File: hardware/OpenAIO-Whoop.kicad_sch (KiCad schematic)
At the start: 0 parts

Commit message: WIP schematic verify (D113): pre-shunt battery node +BATT_IN becomes /POWER/CSA+ (VBAT class) for the lineup power-net style; DRU regenerated; verifier mid-run, not yet final
Co-Authored-By: Claude Opus 5.5 <noreply@anthropic.com>
Claude-Session: https://claude.ai/code/session_01RFaS5jnC9tnPam9GBgmGnG
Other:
- note added: "BATTERY PADS TVS + SHUNT INA186 CURRENT 5V BOOST USB OVP 5V MUX 3V3 LDO CAM 5V FILTER O4 HD SWITCH"
- note added: "MOTOR LANDS LED / BUZZER CAMERA HD (O4) USB JST SH"
- note removed: "BATTERY MOTOR LANDS LED / BUZZER CAMERA HD (O4) USB JST SH"
- note removed: "TVS + SHUNT INA186 CURRENT 5V BOOST USB OVP 5V MUX 3V3 LDO CAM 5V FILTER O4 HD SWITCH"
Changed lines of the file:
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@@
 		)
 	)
-	(text "TVS + SHUNT\nINA186 CURRENT\n5V BOOST\nUSB OVP\n5V MUX\n3V3 LDO\nCAM 5V FILTER\nO4 HD SWITCH"
+	(text "BATTERY PADS\nTVS + SHUNT\nINA186 CURRENT\n5V BOOST\nUSB OVP\n5V MUX\n3V3 LDO\nCAM 5V FILTER\nO4 HD SWITCH"
 		(exclude_from_sim no)
 		(at 20.32 34.29 0)
@@
 		)
 	)
-	(text "BATTERY\nMOTOR LANDS\nLED / BUZZER\nCAMERA\nHD (O4)\nUSB JST SH"
+	(text "MOTOR LANDS\nLED / BUZZER\nCAMERA\nHD (O4)\nUSB JST SH"
 		(exclude_from_sim no)
 		(at 378.46 34.29 0)
@@
 				)
 			)
-			(table_cell "+BATT_IN"
+			(table_cell "CSA+"
 				(exclude_from_sim no)
 				(at 17.78 215.9 0)

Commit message: Schematic fixes: RP2350 UART net names match the hardware UARTs (UART1 on GPIO8/9 = CRSF to the ESP32, UART0 on GPIO16/17 = TX1/RX1 pads); VTX_PWR_CTL on ESP32 GPIO4 (reset pull-down) gets R68 10k pull-up / R84 270R so stock ELRS keeps the VTX on; docs; verify pending
Co-Authored-By: Claude Opus 5.5 <noreply@anthropic.com>
Claude-Session: https://claude.ai/code/session_01RFaS5jnC9tnPam9GBgmGnG
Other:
- sheet PADS ports: added UART0_RX, UART0_TX; removed UART1_RX, UART1_TX
- sheet RX ports: added UART1_RX, UART1_TX; removed UART0_RX, UART0_TX
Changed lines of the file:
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@@
 		)
 	)
-	(label "UART0_TX"
+	(label "UART1_TX"
 		(at 200.66 35.56 0)
 		(effects
@@
 		)
 	)
-	(label "UART1_RX"
+	(label "UART0_RX"
 		(at 358.14 182.88 180)
 		(effects
@@
 		)
 	)
-	(label "UART1_TX"
+	(label "UART0_TX"
 		(at 200.66 180.34 0)
 		(effects
@@
 		)
 	)
-	(label "UART0_RX"
+	(label "UART1_RX"
 		(at 220.98 38.1 180)
 		(effects
@@
 			)
 		)
-		(pin "UART0_TX" input
+		(pin "UART1_TX" input
 			(at 223.52 35.56 180)
 			(effects
@@
 			)
 		)
-		(pin "UART0_RX" output
+		(pin "UART1_RX" output
 			(at 223.52 38.1 180)
 			(effects
@@
 			)
 		)
-		(pin "UART1_TX" input
+		(pin "UART0_TX" input
 			(at 360.68 180.34 180)
 			(effects
@@
 			)
 		)
-		(pin "UART1_RX" output
+		(pin "UART0_RX" output
 			(at 360.68 182.88 180)
 			(effects
@@
 			)
 		)
-		(pin "UART0_TX" output
+		(pin "UART1_TX" output
 			(at 198.12 35.56 0)
 			(effects
@@
 			)
 		)
-		(pin "UART0_RX" input
+		(pin "UART1_RX" input
 			(at 198.12 38.1 0)
 			(effects
@@
 			)
 		)
-		(pin "UART1_TX" output
+		(pin "UART0_TX" output
 			(at 198.12 180.34 0)
 			(effects
@@
 			)
 		)
-		(pin "UART1_RX" input
+		(pin "UART0_RX" input
 			(at 198.12 182.88 0)
 			(effects

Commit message: Schematic readability pass done (graphics only, netlist byte-identical; ERC 0 errors, check_netlist 7/0, independently reviewed); overview MCU block text 12 MHz OSC (D100)
Co-Authored-By: Claude Opus 5.5 <noreply@anthropic.com>
Claude-Session: https://claude.ai/code/session_01RFaS5jnC9tnPam9GBgmGnG
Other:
- note added: "RP2354A CORE SMPS 1V1 12 MHz OSC USB 27R VBAT + CURR ADC BEEPER FET BOOT + SWD VIAS"
- note removed: "RP2354A CORE SMPS 1V1 12 MHz XTAL USB 27R VBAT + CURR ADC BEEPER FET BOOT + SWD VIAS"
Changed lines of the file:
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@@
 		)
 	)
-	(text "RP2354A\nCORE SMPS 1V1\n12 MHz XTAL\nUSB 27R\nVBAT + CURR ADC\nBEEPER FET\nBOOT + SWD VIAS"
+	(text "RP2354A\nCORE SMPS 1V1\n12 MHz OSC\nUSB 27R\nVBAT + CURR ADC\nBEEPER FET\nBOOT + SWD VIAS"
 		(exclude_from_sim no)
 		(at 158.75 40.64 0)

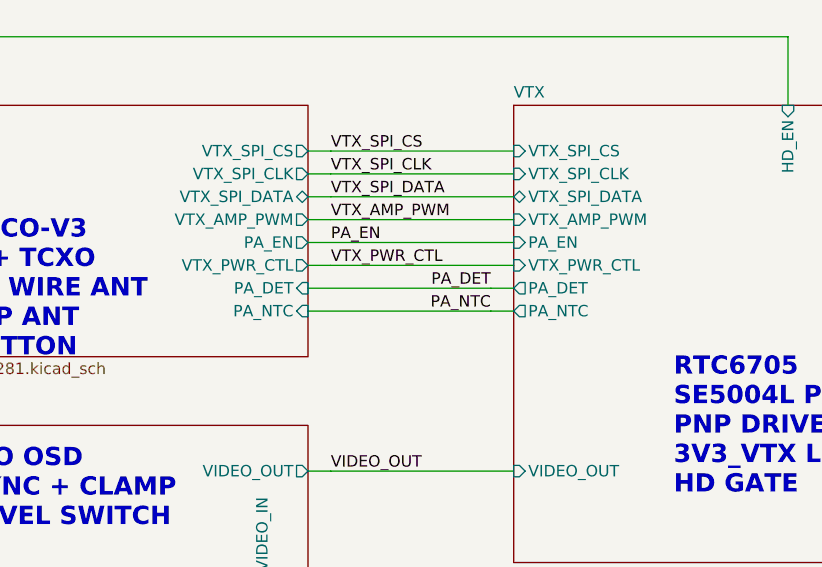
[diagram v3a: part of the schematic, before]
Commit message: Trim BOM to strictly needed parts, fill sourcing fields, fix library datasheets
Owner review 2026-10-11, schematic only (board not resynced).

Removed (17 parts): D1 TVS (clamps above every IC abs max), R2/R3/C5
INA186 input RC, U5 TPS22810 O4 switch with C16/C129/R9/R10/R87/D2
(VHD pad now on +5V_BST, as Matrix HD boards; HD_EN still holds the
analog VTX off via Q28, R11 kept), R67 selector (PA_VCC is +BATT),
TH1/R70 PA NTC and R84 (patched-ELRS only; GPIO37/GPIO4 no-connect),
C92 and C121 (beyond SX1281 / LP5912 datasheet decoupling).

Changed: D4 WS2812 VDD to +5V (3.5 V min); X3 TCXO pin 1 floating per
the YXC sheet; C122/C123/C134 4.7 uF 0402 -> 0201 GRM035R60J475ME15D.

Sourcing: LCSC numbers for 21 MPN lines (SKUBAAE010 has no listing);
every BOM part keeps MPN + Manufacturer for NextPCB.

Library: 16 unused lib symbols pruned; dead or HTML-only datasheet
links replaced with verified PDF URLs (RTC6705, SE5004L, FL2, X1,
EFM8BB51, BC857BM, FTC252012, HCS1206 shunt, Molex 53047).

Net-class patterns and contract entries for the removed nets dropped;
PINMAP ESP32 rows updated (GPIO36 is ADC1_CH0).

Validation: ERC 0 errors / 2 warnings (baseline); check_netlist 7 ok;
sch_integrate --check idempotent; check_conventions unchanged.

Co-Authored-By: Claude Opus 5.5 <noreply@anthropic.com>
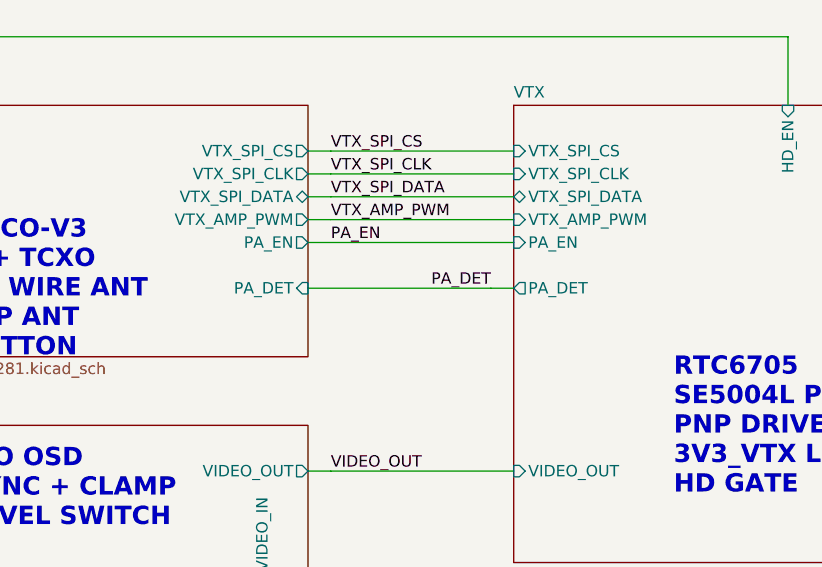
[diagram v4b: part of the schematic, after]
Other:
- sheet RX ports: added none; removed PA_NTC, VTX_PWR_CTL
- sheet VTX ports: added none; removed PA_NTC, VTX_PWR_CTL
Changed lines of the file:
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@@
 	(wire
 		(pts
-			(xy 274.32 53.34) (xy 294.64 53.34)
-		)
-		(stroke
-			(width 0)
-			(type default)
-		)
-	)
-	(wire
-		(pts
 			(xy 139.7 35.56) (xy 142.24 35.56)
 		)
@@
 	(wire
 		(pts
-			(xy 294.64 53.34) (xy 297.18 53.34)
-		)
-		(stroke
-			(width 0)
-			(type default)
-		)
-	)
-	(wire
-		(pts
 			(xy 63.5 101.6) (xy 66.04 101.6)
 		)
@@
 	(wire
 		(pts
-			(xy 274.32 48.26) (xy 276.86 48.26)
-		)
-		(stroke
-			(width 0)
-			(type default)
-		)
-	)
-	(wire
-		(pts
 			(xy 200.66 137.16) (xy 223.52 137.16)
 		)
@@
 	(wire
 		(pts
-			(xy 276.86 48.26) (xy 297.18 48.26)
-		)
-		(stroke
-			(width 0)
-			(type default)
-		)
-	)
-	(wire
-		(pts
 			(xy 114.3 48.26) (xy 139.7 48.26)
 		)
@@
 		)
 	)
-	(label "VTX_PWR_CTL"
-		(at 276.86 48.26 0)
-		(effects
-			(font
-				(size 1.27 1.27)
-			)
-			(justify left bottom)
-		)
-	)
 	(label "VTX_SPI_DATA"
 		(at 276.86 40.64 0)
@@
 		)
 	)
-	(label "PA_NTC"
-		(at 294.64 53.34 180)
-		(effects
-			(font
-				(size 1.27 1.27)
-			)
-			(justify right bottom)
-		)
-	)
 	(label "VIDEO_IN"
 		(at 358.14 88.9 180)
@@
 			)
 		)
-		(pin "VTX_PWR_CTL" input
-			(at 297.18 48.26 180)
-			(effects
-				(font
-					(size 1.27 1.27)
-				)
-				(justify left)
-			)
-		)
 		(pin "PA_DET" output
 			(at 297.18 50.8 180)
@@
 			)
 		)
-		(pin "PA_NTC" output
-			(at 297.18 53.34 180)
-			(effects
-				(font
-					(size 1.27 1.27)
-				)
-				(justify left)
-			)
-		)
 		(pin "VIDEO_OUT" input
 			(at 297.18 71.12 180)
@@
 			)
 		)
-		(pin "VTX_PWR_CTL" output
-			(at 274.32 48.26 0)
-			(effects
-				(font
-					(size 1.27 1.27)
-				)
-				(justify right)
-			)
-		)
 		(pin "PA_DET" input
 			(at 274.32 50.8 0)
 			(effects
 				(font
-					(size 1.27 1.27)
-				)
-				(justify right)
-			)
-		)
-		(pin "PA_NTC" input
-			(at 274.32 53.34 0)
-			(effects
-				(font

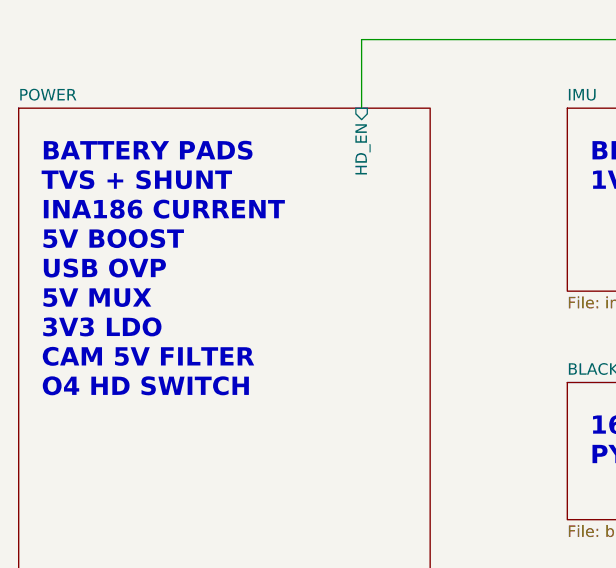
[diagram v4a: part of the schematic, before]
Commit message: 5 V input: two Schottky diodes replace the TPS2116 mux and the SGM40661 (D118)
D9 VBUS -> +5V and D10 +5V_BST -> +5V, MSKSEMI MS2A40LDF DFN1610-2
(LCSC C7380000, imported with import_part.py; land spec PASS). U3, R7,
R8, U24, C131 removed; C128 is +5V bulk; PWR_FLAG on +5V. Board synced.

Stale schematic notes rewritten (O4 switch block now "HD_EN PULL-DOWN",
TVS, INA186 input RC, PA NTC, R67, GPIO4 control, root power table).

ERC 0 errors; check_netlist 7 ok; sch_integrate --check clean;
setup_board --check up to date; board_spec 31/31; sync dry run 0 changes;
DRC unchanged.

Co-Authored-By: Claude Opus 5.5 <noreply@anthropic.com>
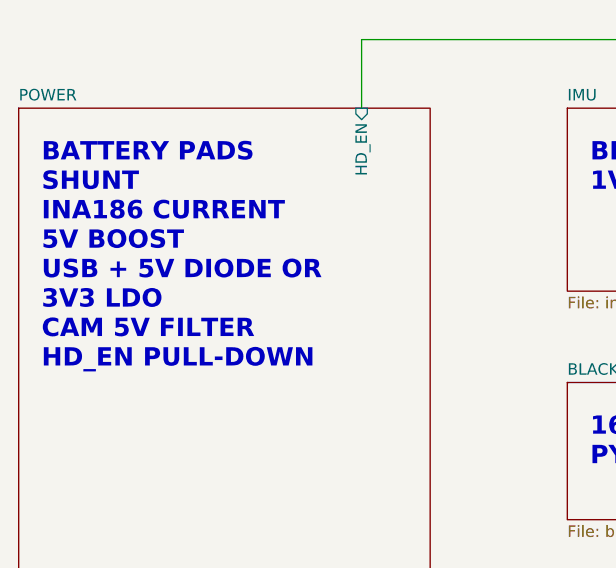
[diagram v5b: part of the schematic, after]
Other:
- note added: "BATTERY PADS SHUNT INA186 CURRENT 5V BOOST USB + 5V DIODE OR 3V3 LDO CAM 5V FILTER HD_EN PULL-DOWN"
- note removed: "BATTERY PADS TVS + SHUNT INA186 CURRENT 5V BOOST USB OVP 5V MUX 3V3 LDO CAM 5V FILTER O4 HD SWITCH"
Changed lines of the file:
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@@
 		)
 	)
-	(text "BATTERY PADS\nTVS + SHUNT\nINA186 CURRENT\n5V BOOST\nUSB OVP\n5V MUX\n3V3 LDO\nCAM 5V FILTER\nO4 HD SWITCH"
+	(text "BATTERY PADS\nSHUNT\nINA186 CURRENT\n5V BOOST\nUSB + 5V DIODE OR\n3V3 LDO\nCAM 5V FILTER\nHD_EN PULL-DOWN"
 		(exclude_from_sim no)
 		(at 20.32 34.29 0)
@@
 				)
 			)
-			(table_cell "TVS, pad bulk, shunt R1"
+			(table_cell "pad bulk, shunt R1"
 				(exclude_from_sim no)
 				(at 170.18 215.9 0)
@@
 				)
 			)
-			(table_cell "ESC1-4, boost, O4 EN, VBAT ADC, PA_VCC"
+			(table_cell "ESC1-4, boost, VBAT ADC, SE5004L VCC"
 				(exclude_from_sim no)
 				(at 170.18 219.71 0)
@@
 				)
 			)
-			(table_cell "+5V_USB"
+			(table_cell "VBUS -> +5V"
 				(exclude_from_sim no)
 				(at 17.78 227.33 0)
@@
 				)
 			)
-			(table_cell "U24 SGM40661 OVP"
+			(table_cell "D9 Schottky"
 				(exclude_from_sim no)
 				(at 40.64 227.33 0)
@@
 				)
 			)
-			(table_cell "U3 VIN2, U5 O4 switch"
+			(table_cell "D10 to +5V, VHD pad (O4)"
 				(exclude_from_sim no)
 				(at 170.18 231.14 0)
@@
 				)
 			)
-			(table_cell "U3 TPS2116 mux"
+			(table_cell "D9 / D10 diode-OR"
 				(exclude_from_sim no)
 				(at 40.64 234.95 0)
@@
 				)
 			)
-			(table_cell "+5V_HD"
+			(table_cell "(VHD on +5V_BST)"
 				(exclude_from_sim no)
 				(at 17.78 242.57 0)
@@
 				)
 			)
-			(table_cell "U5 TPS22810 (HD_EN, cell)"
+			(table_cell "no switch (D114)"
 				(exclude_from_sim no)
 				(at 40.64 242.57 0)
@@
 				)
 			)
-			(table_cell "R67 selector, +BATT default"
+			(table_cell "+BATT direct (D114)"
 				(exclude_from_sim no)
 				(at 40.64 261.62 0)

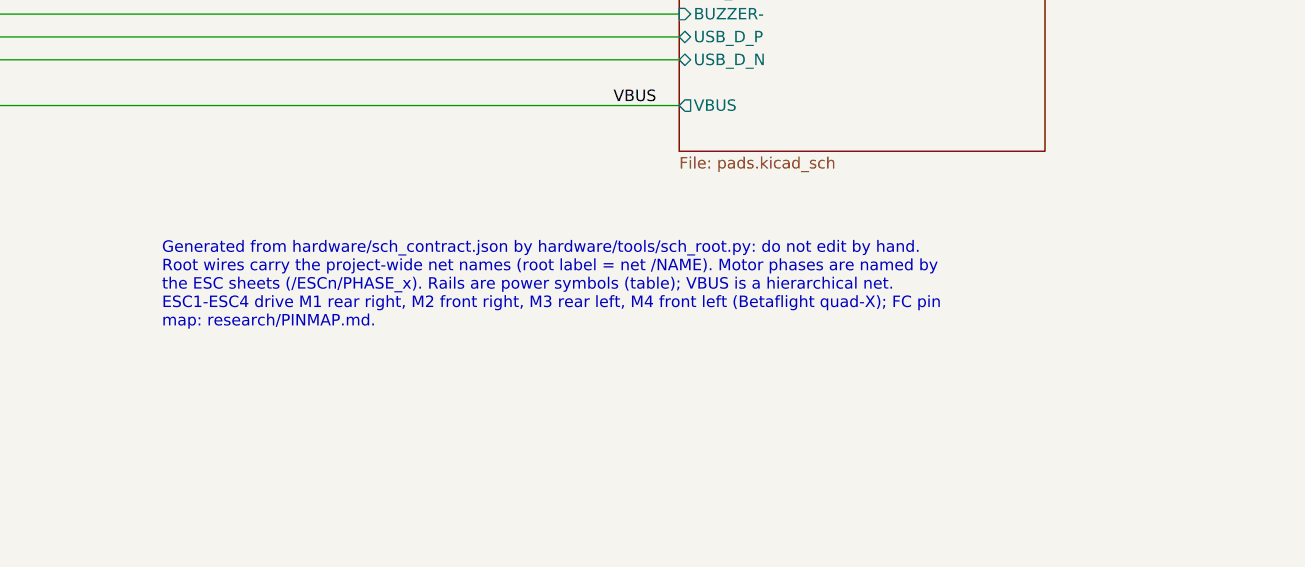
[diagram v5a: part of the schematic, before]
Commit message: Footprint audit vs datasheets, 0201 lands to Murata minimum, schematic notes shortened
Footprints: 45 checked against their datasheets by group, no pin or
land errors. C/R/L_0201_..._L pad height 0.28 -> 0.30 (Murata GRM03
reflow table c >= 0.30); other lands already at least density per D109
and left unchanged. Land spec texts cleaned (sources, shared parts).

Schematic notes: 157 -> 152 items, 19.5k -> 9.7k characters, all
current (diode-OR, removed parts, RTC6705 filters, TX0/RX0).

check_footprint 107/107 lib specs PASS; ERC 0 errors / 2 warnings;
check_netlist 7 ok; sch_integrate --check clean. Board not synced.

Co-Authored-By: Claude Opus 5.5 <noreply@anthropic.com>
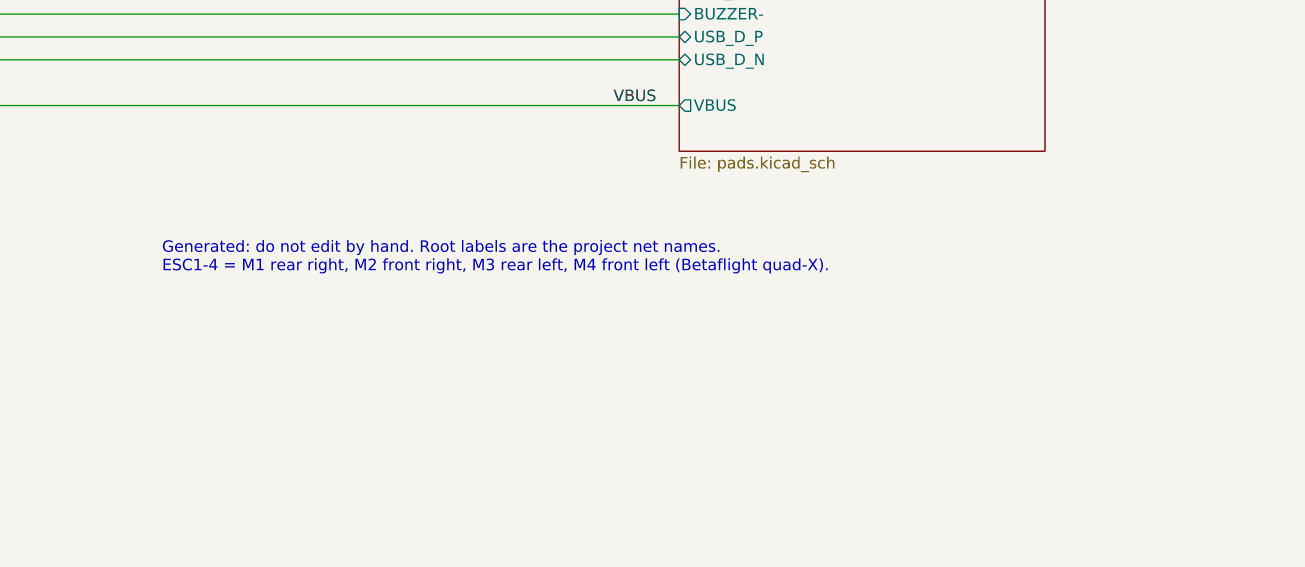
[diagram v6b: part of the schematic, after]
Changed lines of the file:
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@@
 		)
 	)
-	(text_box "Generated from hardware/sch_contract.json by hardware/tools/sch_root.py: do not edit by hand.\nRoot wires carry the project-wide net names (root label = net /NAME). Motor phases are named by the ESC sheets (/ESCn/PHASE_x). Rails are power symbols (table); VBUS is a hierarchical net.\nESC1-ESC4 drive M1 rear right, M2 front right, M3 rear left, M4 front left (Betaflight quad-X); FC pin map: research/PINMAP.md."
+	(text_box "Generated: do not edit by hand. Root labels are the project net names.\nESC1-4 = M1 rear right, M2 front right, M3 rear left, M4 front left (Betaflight quad-X)."
 		(exclude_from_sim no)
 		(at 302.26 212.09 0)

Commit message: WIP placement and schematic snapshot for shared routing
Owner placement and schematic edits, firmware bindings, routing notes and
board tooling, so others can try the routing. Not DRC-clean; PCB not yet
updated from the schematic (R1 to R2, C1/C2/C134 removal).

Co-Authored-By: Claude Opus 5.5 <noreply@anthropic.com>
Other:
- sheet POWER ports: added none; removed HD_EN
- note added: "BATTERY PADS SHUNT INA186 CURRENT 5V BOOST USB + 5V DIODE OR 3V3 LDO CAM 5V FILTER REVERSE BYPASS"
- note removed: "BATTERY PADS SHUNT INA186 CURRENT 5V BOOST USB + 5V DIODE OR 3V3 LDO CAM 5V FILTER HD_EN PULL-DOWN"
